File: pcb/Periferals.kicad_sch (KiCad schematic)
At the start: 24 parts, among them J14 Micro_SD_Card_passive_clk, U5 MCP23017x-x-SS

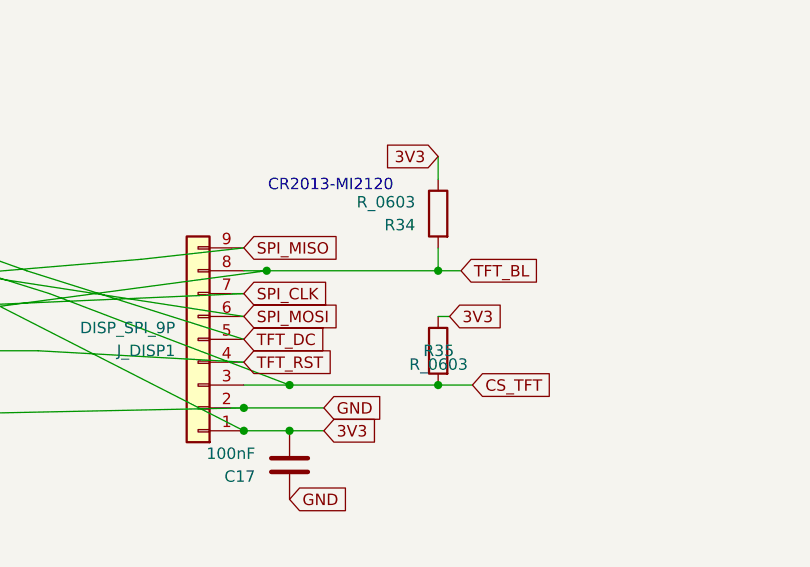
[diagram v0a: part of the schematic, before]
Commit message: adds licences, top level readme
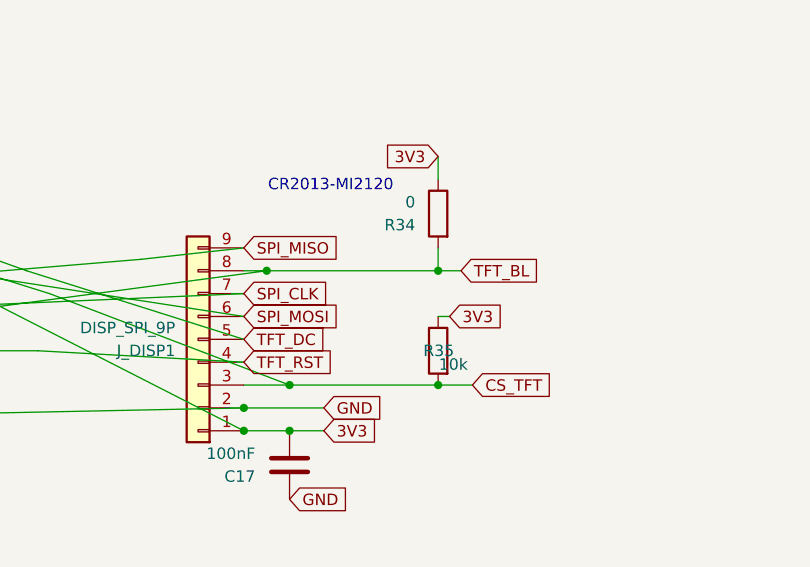
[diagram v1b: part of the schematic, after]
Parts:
- R34: value R_0603 -> 0
- R35: value R_0603 -> 10k
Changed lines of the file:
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@@
 			)
 		)
-		(property "Value" "R_0603"
+		(property "Value" "0"
 			(at 123.19 118.1101 0)
 			(show_name no)
@@
 			)
 		)
-		(property "Value" "R_0603"
+		(property "Value" "10k"
 			(at 129.032 136.144 0)
 			(show_name no)
